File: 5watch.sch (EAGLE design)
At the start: 33 parts, among them U1 ATMEGA328P_TQFP, Y2 32.768 kHz

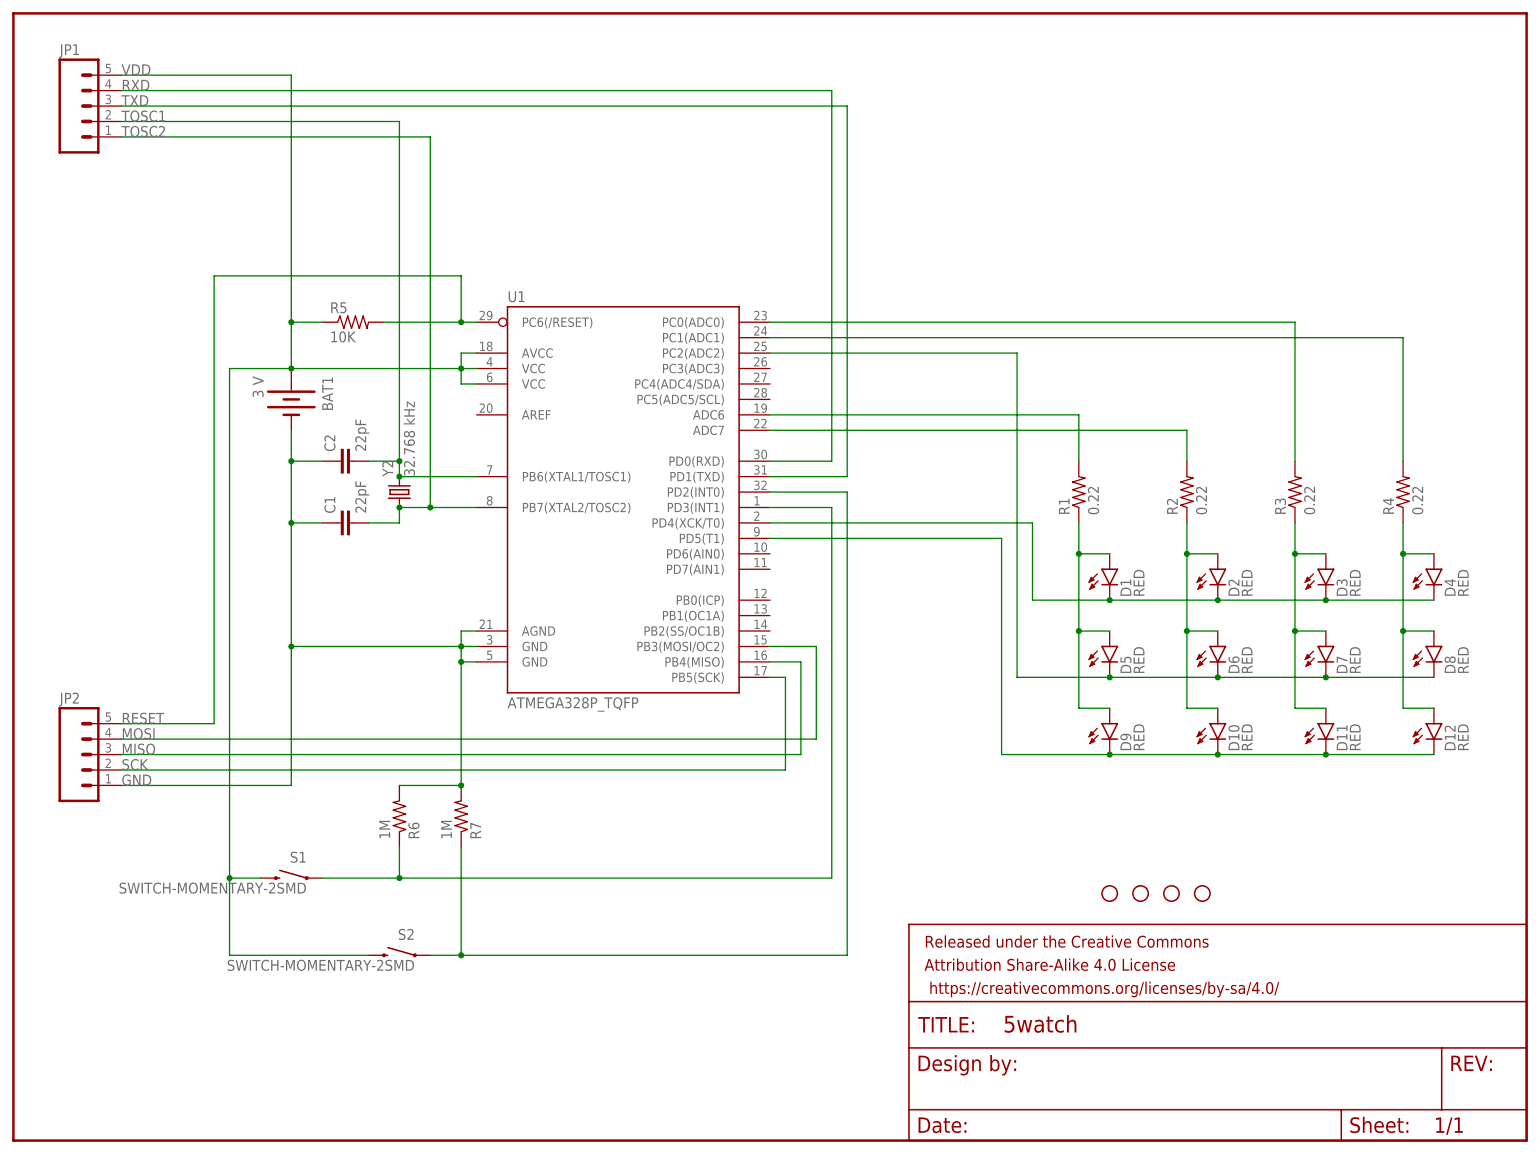
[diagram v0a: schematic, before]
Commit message: fixed led connections, wired ADC6 and ADC7 to ground, removed TOSC pins from breakout, shrunk board, reversed button pin voltages
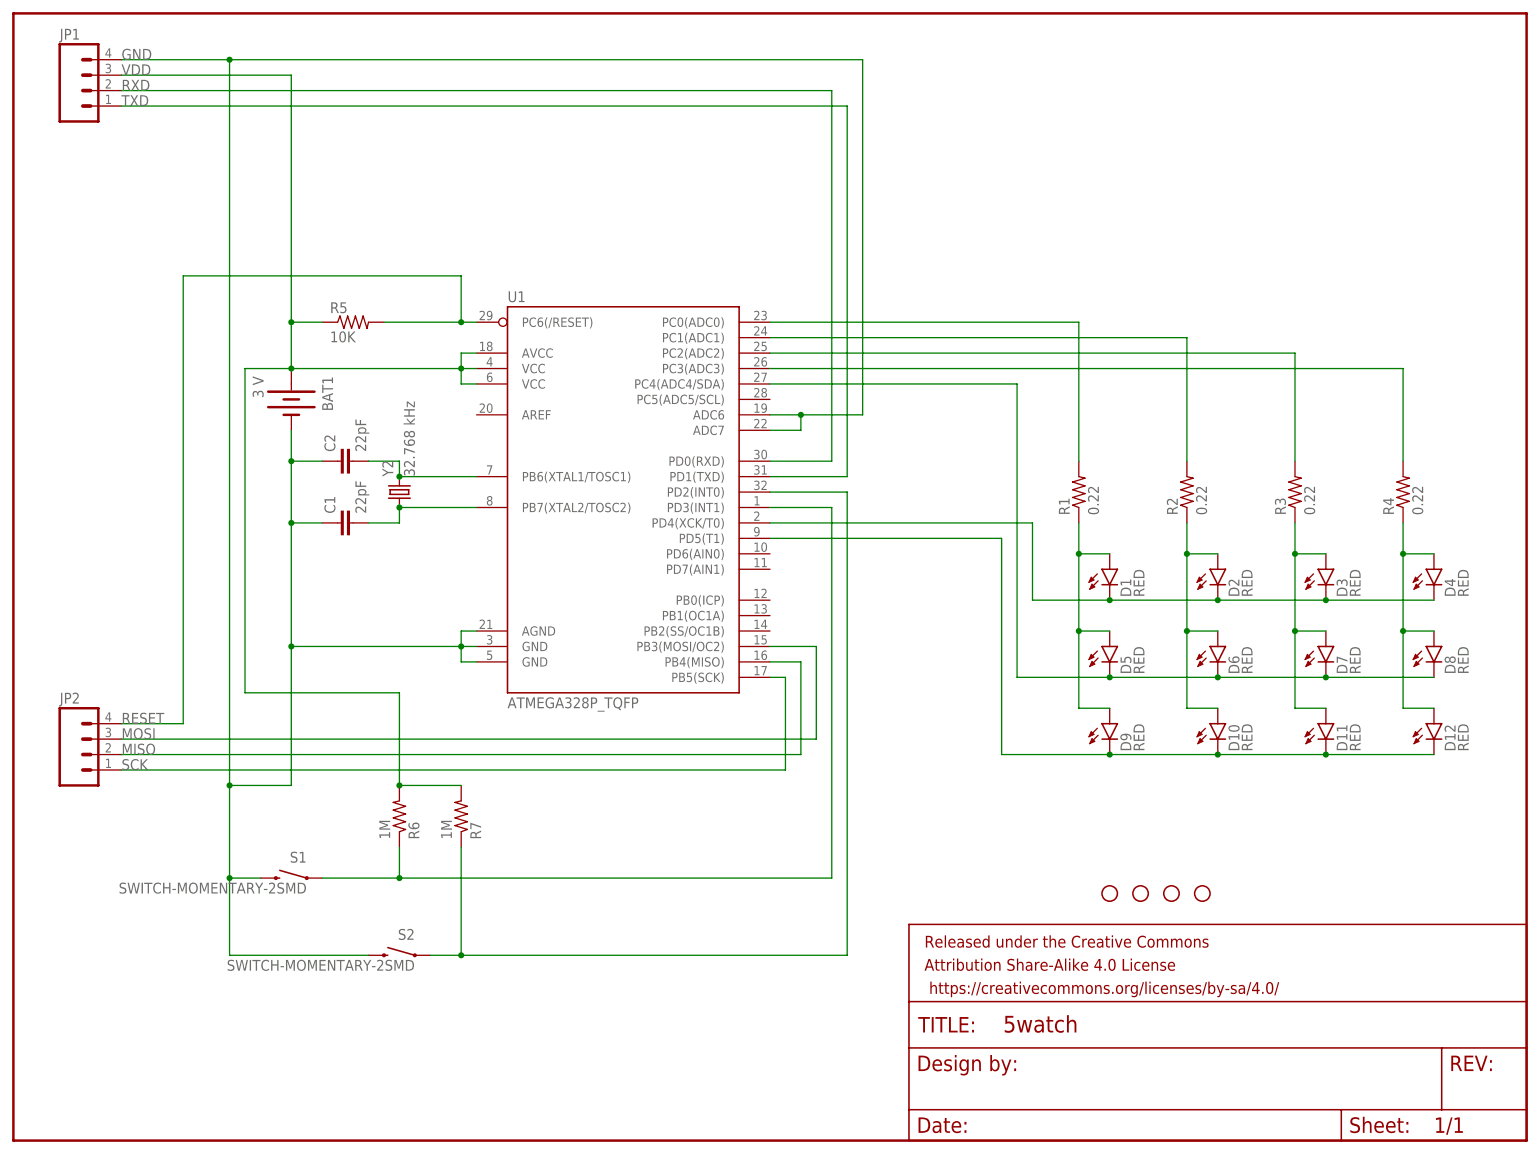
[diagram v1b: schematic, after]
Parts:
- JP1, JP2: device SparkFun-Connectors:M05PTH -> SparkFun-Connectors:M04NO_SILK_ALL_ROUND
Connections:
- removed net TOSC1: C2.2, JP1.2, U1.PB6(XTAL1/TOSC1), Y2.2
- removed net TOSC2: C1.2, JP1.1, U1.PB7(XTAL2/TOSC2), Y2.1
- new net N$10: C1.2, U1.PB7(XTAL2/TOSC2), Y2.1
- new net N$8: C2.2, U1.PB6(XTAL1/TOSC1), Y2.2
- net GND: now also JP1.4, S1.2, S2.2, U1.ADC6, U1.ADC7; no longer JP2.1, R6.2, R7.2
- net MISO: now also JP2.2; no longer JP2.3
- net MOSI: now also JP2.3; no longer JP2.4
- net N$13: now also U1.PC3(ADC3); no longer U1.PC1(ADC1)
- net N$19: now also U1.PC2(ADC2); no longer U1.PC0(ADC0)
- net N$20: now also U1.PC1(ADC1); no longer U1.ADC7
- net N$21: now also U1.PC0(ADC0); no longer U1.ADC6
- net N$6: now also U1.PC4(ADC4/SDA); no longer U1.PC2(ADC2)
- net RESET: now also JP2.4; no longer JP2.5
- net RXD: now also JP1.2; no longer JP1.4
- net SCK: now also JP2.1; no longer JP2.2
- net TXD: now also JP1.1; no longer JP1.3
- net VDD: now also JP1.3, R6.2, R7.2; no longer JP1.5, S1.2, S2.2
